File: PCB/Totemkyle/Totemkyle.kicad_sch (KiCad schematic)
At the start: 88 parts, among them U1 xiao-ble, U2 xiao-ble

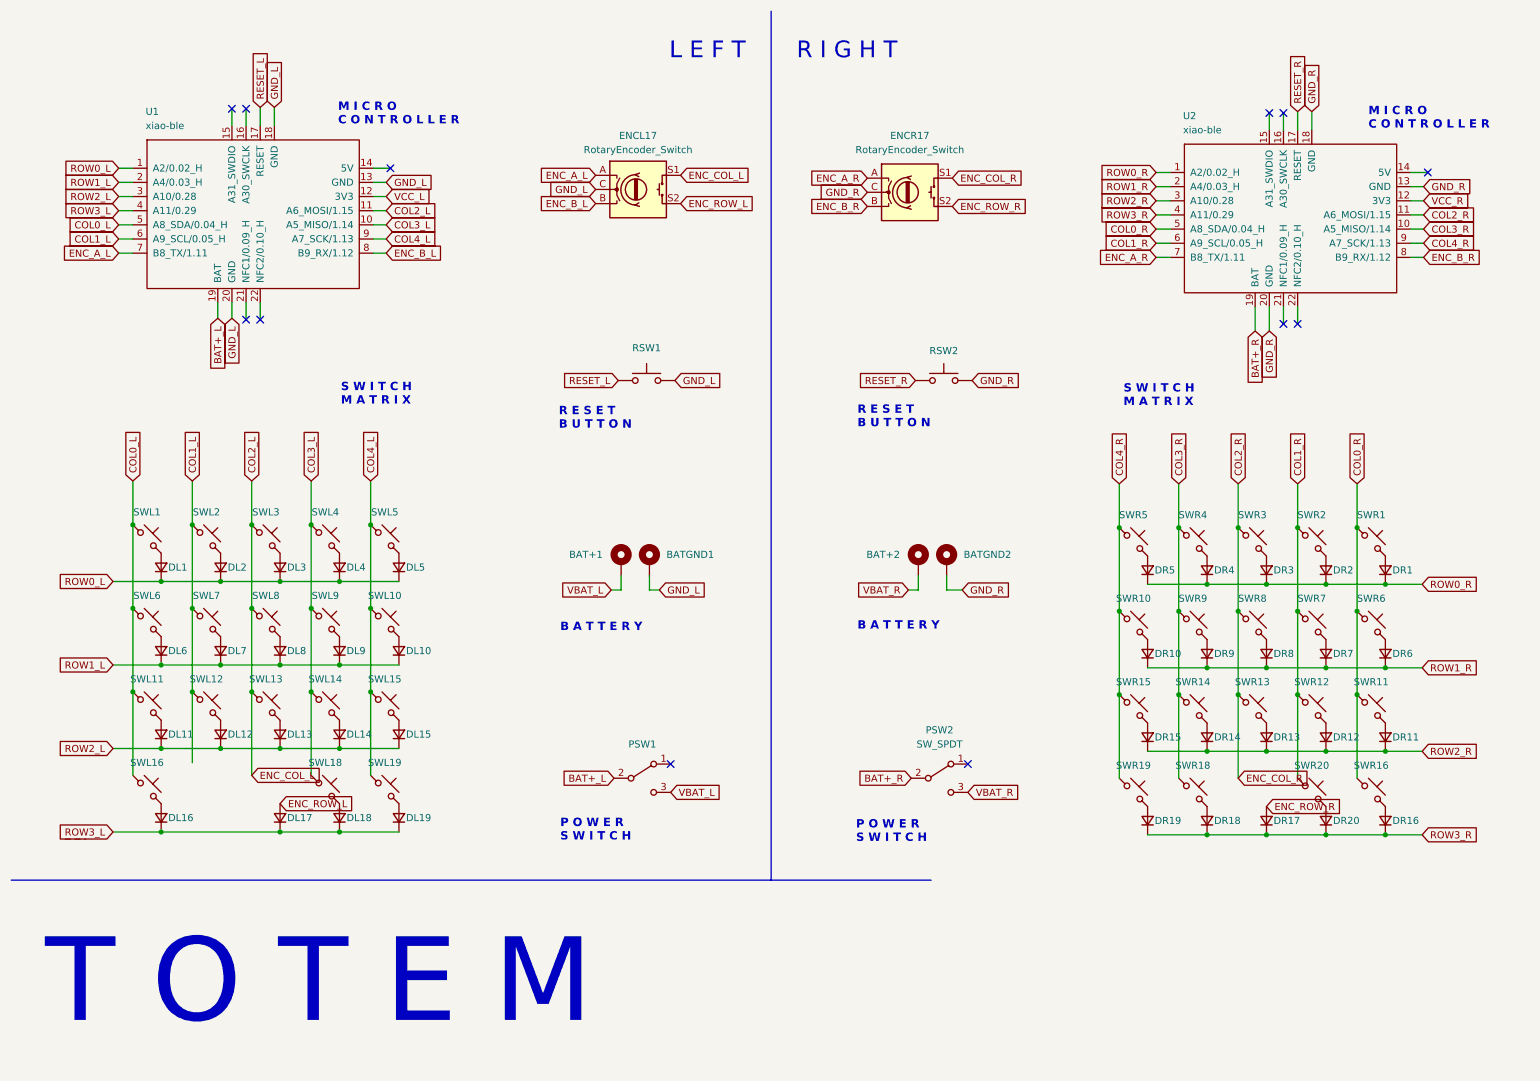
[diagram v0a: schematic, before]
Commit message: Add 1 key and roller encoder
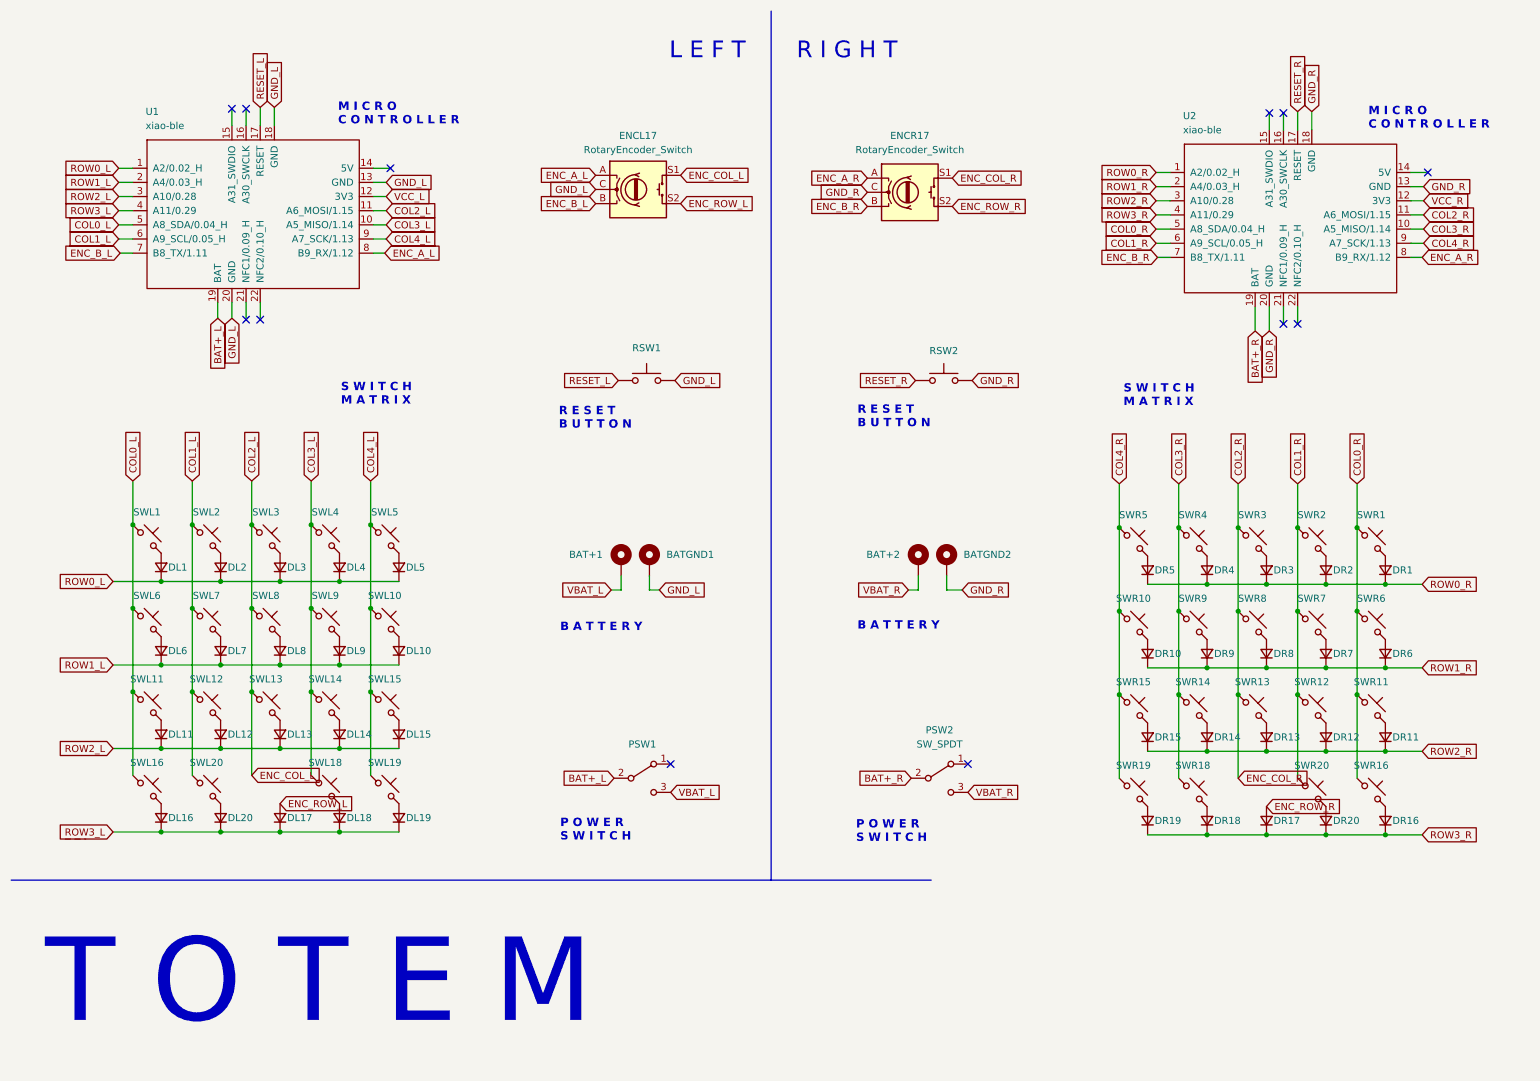
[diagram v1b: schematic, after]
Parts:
- added DL20: D_Small, TOTEMlib:Diode_SOD123, symbol Device:D_Small
- added SWL20: SW_Push_45deg, TOTEMlib:Kailh_socket_PG1350, symbol Switch:SW_Push_45deg
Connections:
- net COL1_L: now also SWL20.1
- net ENC_A_L: now also U1.8 (B9_RX/1.12); no longer U1.7 (B8_TX/1.11)
- net ENC_A_R: now also U2.8 (B9_RX/1.12); no longer U2.7 (B8_TX/1.11)
- net ENC_B_L: now also U1.7 (B8_TX/1.11); no longer U1.8 (B9_RX/1.12)
- net ENC_B_R: now also U2.7 (B8_TX/1.11); no longer U2.8 (B9_RX/1.12)
- net ROW3_L: now also DL20.1 (K)
- new net: DL20.2 (A), SWL20.2
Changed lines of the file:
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@@
 	)
 	(junction
+		(at 49.53 159.258)
+		(diameter 0)
+		(color 0 0 0 0)
+	)
+	(junction
 		(at 55.118 119.126)
 		(diameter 0)
@@
 	(wire
 		(pts
+			(xy 49.53 159.258) (xy 60.198 159.258)
+		)
+		(stroke
+			(width 0)
+			(type default)
+		)
+	)
+	(wire
+		(pts
 			(xy 247.904 114.808) (xy 258.572 114.808)
 		)
@@
 	(wire
 		(pts
-			(xy 217.424 56.134) (xy 219.964 56.134)
-		)
-		(stroke
-			(width 0)
-			(type default)
-		)
-	)
-	(wire
-		(pts
 			(xy 70.866 129.286) (xy 81.534 129.286)
 		)
@@
 	(wire
 		(pts
+			(xy 265.176 56.134) (xy 263.144 56.134)
+		)
+		(stroke
+			(width 0)
+			(type default)
+		)
+	)
+	(wire
+		(pts
 			(xy 55.118 134.112) (xy 55.118 149.098)
 		)
@@
 	(wire
 		(pts
+			(xy 217.678 56.134) (xy 219.964 56.134)
+		)
+		(stroke
+			(width 0)
+			(type default)
+		)
+	)
+	(wire
+		(pts
 			(xy 38.862 129.286) (xy 49.53 129.286)
 		)
@@
 	(wire
 		(pts
-			(xy 237.744 65.024) (xy 237.744 69.342)
+			(xy 44.45 134.112) (xy 44.45 149.098)
 		)
 		(stroke
@@
 	(wire
 		(pts
-			(xy 76.962 52.832) (xy 79.248 52.832)
+			(xy 237.744 65.024) (xy 237.744 69.342)
 		)
 		(stroke
@@
 	(wire
 		(pts
-			(xy 253.492 104.648) (xy 253.492 119.634)
+			(xy 76.962 52.832) (xy 79.248 52.832)
 		)
 		(stroke
@@
 	(wire
 		(pts
-			(xy 38.862 144.272) (xy 49.53 144.272)
+			(xy 253.492 104.648) (xy 253.492 119.634)
 		)
 		(stroke
@@
 	(wire
 		(pts
-			(xy 51.562 29.464) (xy 51.562 32.512)
+			(xy 38.862 144.272) (xy 49.53 144.272)
 		)
 		(stroke
@@
 	(wire
 		(pts
-			(xy 76.962 55.372) (xy 79.248 55.372)
+			(xy 51.562 29.464) (xy 51.562 32.512)
 		)
 		(stroke
@@
 	(wire
 		(pts
-			(xy 263.144 56.134) (xy 265.43 56.134)
-		)
-		(stroke
-			(width 0)
-			(type default)
-		)
-	)
-	(wire
-		(pts
-			(xy 44.45 146.812) (xy 44.45 134.112)
-		)
-		(stroke
-			(width 0)
-			(type default)
-		)
-	)
-	(wire
-		(pts
 			(xy 263.144 40.894) (xy 266.192 40.894)
 		)
@@
 	(wire
 		(pts
+			(xy 78.994 55.372) (xy 76.962 55.372)
+		)
+		(stroke
+			(width 0)
+			(type default)
+		)
+	)
+	(wire
+		(pts
 			(xy 76.454 119.126) (xy 76.454 134.112)
 		)
@@
 	(wire
 		(pts
+			(xy 31.496 55.372) (xy 33.782 55.372)
+		)
+		(stroke
+			(width 0)
+			(type default)
+		)
+	)
+	(wire
+		(pts
 			(xy 59.182 29.21) (xy 59.182 32.512)
 		)
@@
 	(wire
 		(pts
-			(xy 31.242 55.372) (xy 33.782 55.372)
-		)
-		(stroke
-			(width 0)
-			(type default)
-		)
-	)
-	(wire
-		(pts
 			(xy 44.45 104.14) (xy 44.45 119.126)
 		)
@@
 	(wire
 		(pts
-			(xy 38.862 159.258) (xy 60.198 159.258)
+			(xy 38.862 159.258) (xy 49.53 159.258)
 		)
 		(stroke
@@
 	(global_label "ENC_B_L"
 		(shape input)
-		(at 79.248 55.372 0)
+		(at 31.496 55.372 180)
 		(fields_autoplaced yes)
 		(effects
@@
 				(size 1.27 1.27)
 			)
-			(justify left)
+			(justify right)
 		)
 		(property "Intersheetrefs" "${INTERSHEET_REFS}"
-			(at 90.216 55.372 0)
+			(at 20.528 55.372 0)
 			(effects
 				(font
 					(size 1.27 1.27)
 				)
-				(justify left)
+				(justify right)
 				(hide yes)
 			)
@@
 	(global_label "ENC_A_R"
 		(shape input)
-		(at 217.424 56.134 180)
+		(at 265.176 56.134 0)
 		(fields_autoplaced yes)
 		(effects
@@
 				(size 1.27 1.27)
 			)
-			(justify right)
+			(justify left)
 		)
 		(property "Intersheetrefs" "${INTERSHEET_REFS}"
-			(at 206.3955 56.134 0)
+			(at 276.2045 56.134 0)
 			(effects
 				(font
 					(size 1.27 1.27)
 				)
-				(justify right)
+				(justify left)
 				(hide yes)
 			)
@@
 	(global_label "ENC_B_R"
 		(shape input)
-		(at 265.43 56.134 0)
+		(at 217.678 56.134 180)
 		(fields_autoplaced yes)
 		(effects
@@
 				(size 1.27 1.27)
 			)
-			(justify left)
+			(justify right)
 		)
 		(property "Intersheetrefs" "${INTERSHEET_REFS}"
-			(at 276.6399 56.134 0)
+			(at 206.4681 56.134 0)
 			(effects
 				(font
 					(size 1.27 1.27)
 				)
-				(justify left)
+				(justify right)
 				(hide yes)
 			)
@@
 	(global_label "ENC_A_L"
 		(shape input)
-		(at 31.242 55.372 180)
+		(at 78.994 55.372 0)
 		(fields_autoplaced yes)
 		(effects
@@
 				(size 1.27 1.27)
 			)
-			(justify right)
+			(justify left)
 		)
 		(property "Intersheetrefs" "${INTERSHEET_REFS}"
-			(at 20.4554 55.372 0)
+			(at 89.7806 55.372 0)
 			(effects
 				(font
 					(size 1.27 1.27)
 				)
-				(justify right)
+				(justify left)
 				(hide yes)
 			)
@@
 	)
 	(symbol
+		(lib_id "Device:D_Small")
+		(at 49.53 156.718 90)
+		(unit 1)
+		(exclude_from_sim no)
+		(in_bom yes)
+		(on_board yes)
+		(dnp no)
+		(property "Reference" "DL20"
+			(at 50.8 156.718 90)
+			(effects
+				(font
+					(size 1.27 1.27)
+				)
+				(justify right)
+			)
+		)
+		(property "Value" "D_Small"
+			(at 52.324 157.9879 90)
+			(effects
+				(font
+					(size 1.27 1.27)
+				)
+				(justify right)
+				(hide yes)
+			)
+		)
+		(property "Footprint" "TOTEMlib:Diode_SOD123"
+			(at 49.53 156.718 90)
+			(effects
+				(font
+					(size 1.27 1.27)
+				)
+				(hide yes)
+			)
+		)
+		(property "Datasheet" "~"
+			(at 49.53 156.718 90)
+			(effects
+				(font
+					(size 1.27 1.27)
+				)
+				(hide yes)
+			)
+		)
+		(property "Description" ""
+			(at 49.53 156.718 0)
+			(effects
+				(font
+					(size 1.27 1.27)
+				)
+			)
+		)
+		(pin "1"
+		)
+		(pin "2"
+		)
+		(instances
+			(project "Totemkyle"
+				(path "/4d1e609f-5432-4afb-8ee7-7d2d9aaaee48"
+					(reference "DL20")
+					(unit 1)
+				)
+			)
+		)
+	)
+	(symbol
 		(lib_id "Mechanical:MountingHole_Pad")
 		(at 179.832 110.744 0)
@@
 					(unit 1)
 				)
+			)
+		)
+	)
+	(symbol
+		(lib_id "Switch:SW_Push_45deg")
+		(at 46.99 151.638 0)
+		(unit 1)
+		(exclude_from_sim no)
+		(in_bom yes)
+		(on_board yes)
+		(dnp no)
+		(property "Reference" "SWL20"
+			(at 46.99 146.812 0)
+			(effects
+				(font
+					(size 1.27 1.27)
+				)
+			)
+		)
+		(property "Value" "SW_Push_45deg"
+			(at 46.99 146.05 0)
+			(effects
+				(font
+					(size 1.27 1.27)
+				)
+				(hide yes)
+			)
+		)
+		(property "Footprint" "TOTEMlib:Kailh_socket_PG1350"
+			(at 46.99 151.638 0)
+			(effects
+				(font
+					(size 1.27 1.27)
+				)
+				(hide yes)
+			)
+		)
+		(property "Datasheet" "~"
+			(at 46.99 151.638 0)
+			(effects
+				(font
+					(size 1.27 1.27)
+				)
+				(hide yes)
+			)
+		)
+		(property "Description" ""
+			(at 46.99 151.638 0)
+			(effects
+				(font
+					(size 1.27 1.27)
+				)
+			)
+		)
+		(pin "1"
+		)
+		(pin "2"
+		)
+		(instances
+			(project "Totemkyle"
+				(path "/4d1e609f-5432-4afb-8ee7-7d2d9aaaee48"
+					(reference "SWL20")
+					(unit 1)
+				)
